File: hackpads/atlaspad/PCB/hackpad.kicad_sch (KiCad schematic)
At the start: 54 parts, among them SW1 Keyswitch, SW10 Keyswitch, SW11 Keyswitch, SW12 Keyswitch, SW13 EC05E1220203, SW14 EC05E1220203, SW2 Keyswitch, SW3 Keyswitch, SW4 Keyswitch, SW5 Keyswitch, SW6 Keyswitch, SW7 Keyswitch, SW8 Keyswitch, SW9 Keyswitch, U1 XIAO-RP2040-DIP, U2 DM-OLED096-636, U3 SN74LV1T34DBV

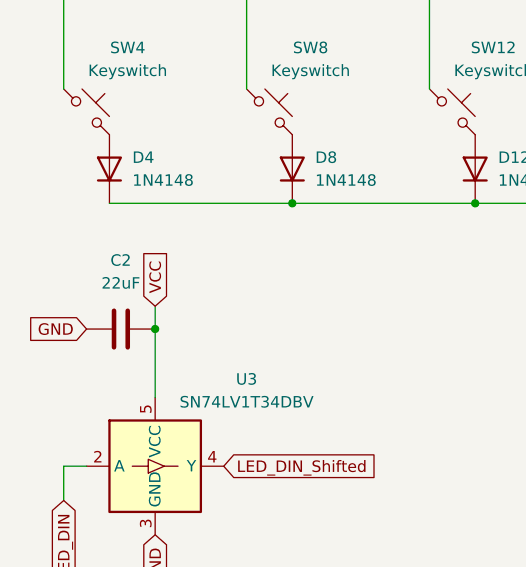
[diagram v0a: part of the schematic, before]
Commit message: added schematic Screenshot and changed C1 to 10uF
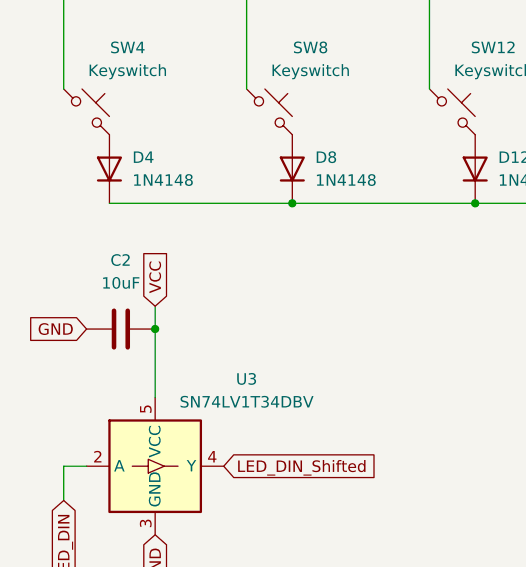
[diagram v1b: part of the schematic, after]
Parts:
- C2: value 22uF -> 10uF
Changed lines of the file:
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@@
 (kicad_sch
-	(version 20231120)
+	(version 20250114)
 	(generator "eeschema")
-	(generator_version "8.0")
+	(generator_version "9.0")
 	(paper "A4")
 	(junction
@@
 			)
 		)
-		(property "Value" "22uF"
+		(property "Value" "10uF"
 			(at 31.75 132.08 90)
 			(effects
@@
 		)
 	)
+	(embedded_fonts no)
 )
